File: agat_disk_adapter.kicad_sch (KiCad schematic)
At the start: 10 parts, among them J1 КОНТРОЛЛЕР, J2_A1 ИЗОТ, J2_B2 ИЗОТ, J3 DISK II, J4 GOTEK, J5 Питание GOTEK, J6 ВБ, J7 Джамперы, J8 ВБ2

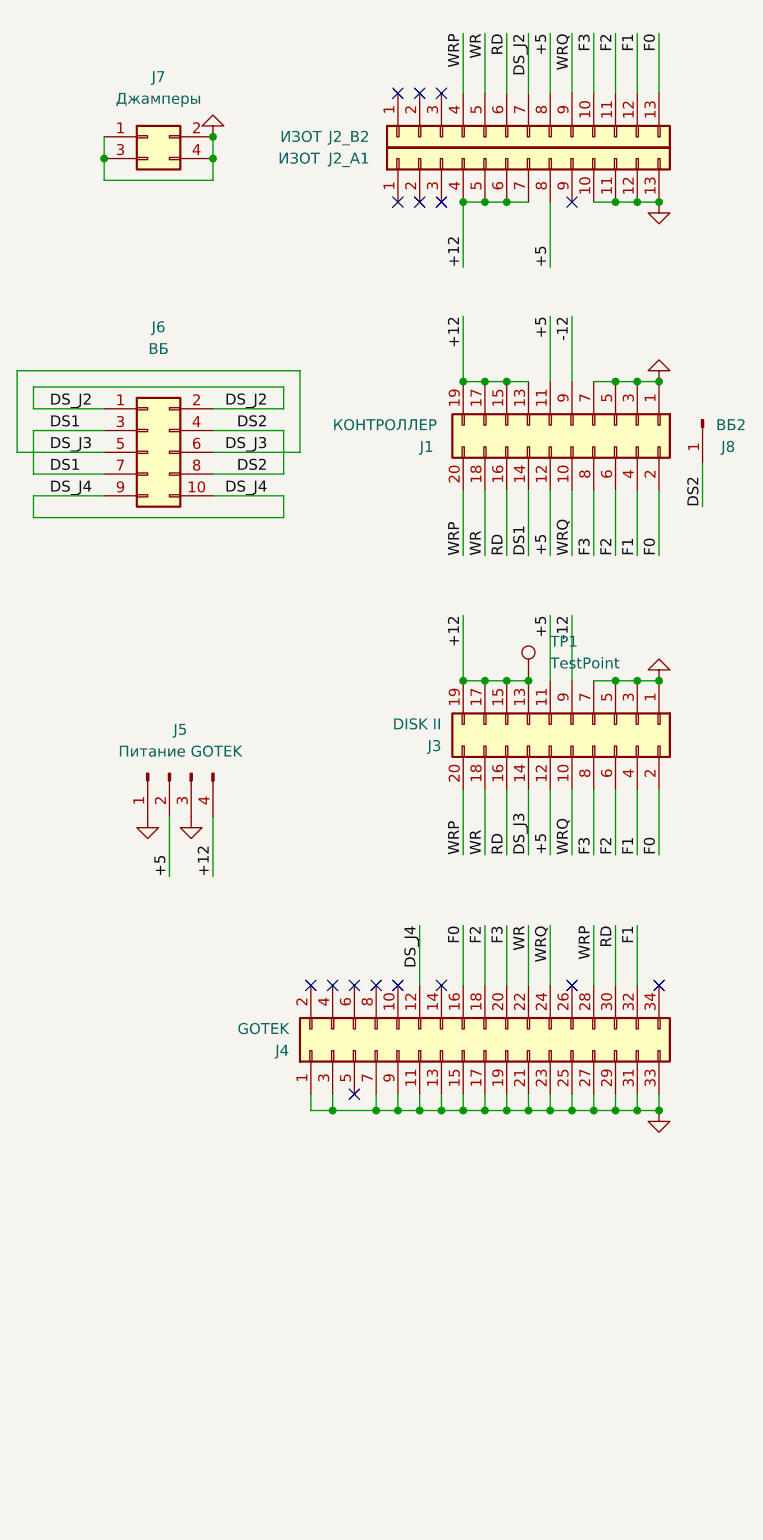
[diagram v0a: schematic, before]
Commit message: one fdc connector
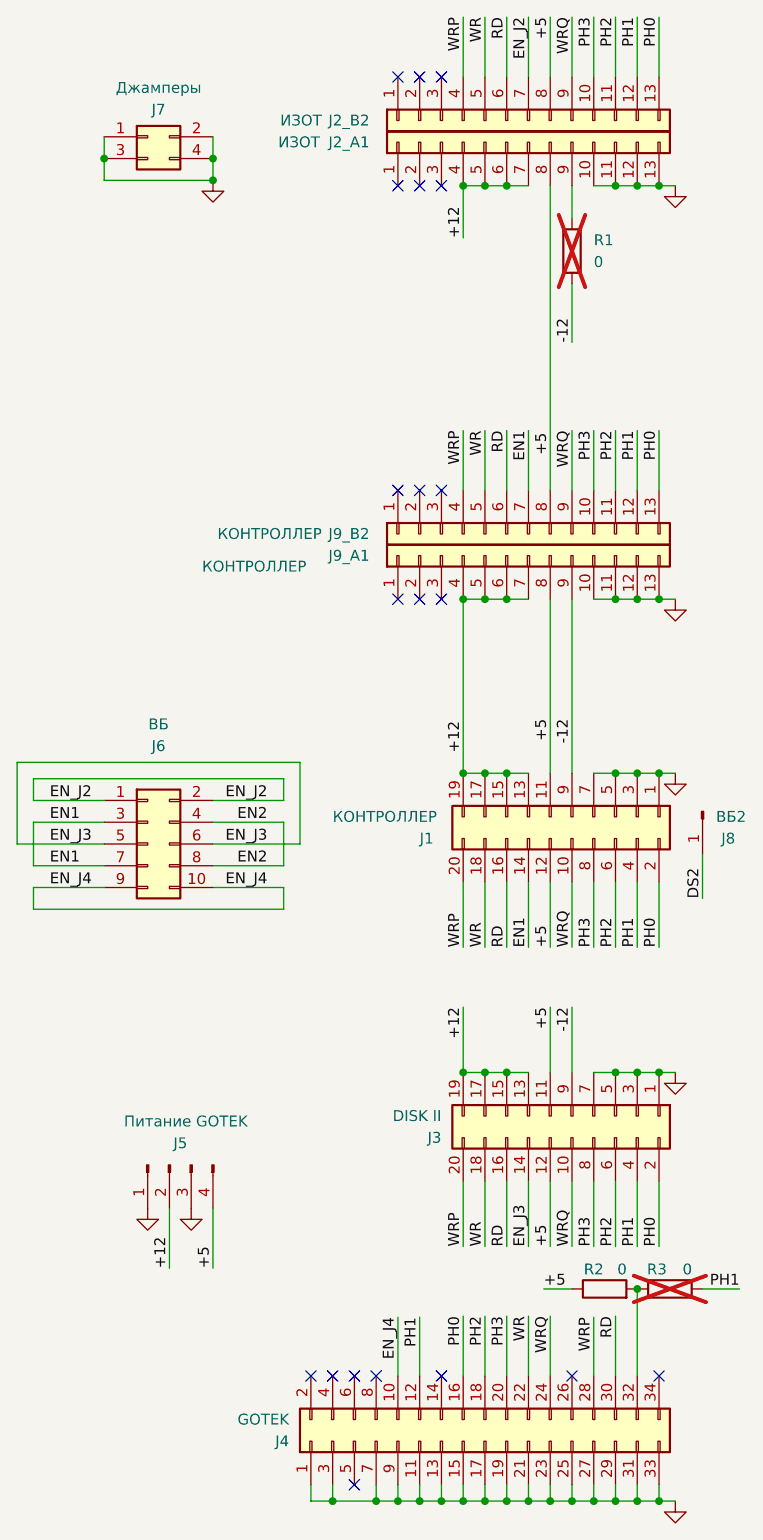
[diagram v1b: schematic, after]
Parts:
- removed TP1: TestPoint, TestPoint:TestPoint_Pad_D3.0mm, symbol Connector:TestPoint
- added J9_A1, J9_B2: КОНТРОЛЛЕР, Connector_JST:JST_EH_B13B-EH-A_1x13_P2.50mm_Vertical, symbol Connector_Generic:Conn_01x13
- added R1, R2, R3: 0, Resistor_SMD:R_1206_3216Metric, symbol Device:R
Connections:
- net +12: now also J5.2 (Pin_2), J9_A1.4 (Pin_4), J9_A1.5 (Pin_5), J9_A1.6 (Pin_6), J9_A1.7 (Pin_7); no longer J5.4 (Pin_4)
- net +5: now also J5.4 (Pin_4), J9_A1.8 (Pin_8), J9_B2.8 (Pin_8), R2.1; no longer J5.2 (Pin_2)
- net -12: now also J9_A1.9 (Pin_9), R1.2
- net DS2: no longer J6.4 (Pin_4), J6.8 (Pin_8)
- net GND: now also J9_A1.10 (Pin_10), J9_A1.11 (Pin_11), J9_A1.12 (Pin_12), J9_A1.13 (Pin_13)
- net RD: now also J9_B2.6 (Pin_6)
- net WR: now also J9_B2.5 (Pin_5)
- net WRP: now also J9_B2.4 (Pin_4)
- net WRQ: now also J9_B2.9 (Pin_9)
- net EN_J4: now reaches J4.10 (Pin_10)
- net EN_J4: now also J6.10 (Pin_10), J6.9 (Pin_9)
- net at J2_A1.9 (Pin_9): now also R1.1
- net DS1 renamed EN1
- net EN1: now also J9_B2.7 (Pin_7)
- net DS_J2 renamed EN_J2
- net DS_J3 renamed EN_J3
- removed net DS_J4: J4.12 (Pin_12), J6.10 (Pin_10), J6.9 (Pin_9)
- net F0 renamed PH0
- net PH0: now also J9_B2.13 (Pin_13)
- net F1 renamed PH1
- net PH1: now also J4.12 (Pin_12), J9_B2.12 (Pin_12), R3.1; no longer J4.32 (Pin_32)
- net F2 renamed PH2
- net PH2: now also J9_B2.11 (Pin_11)
- net F3 renamed PH3
- net PH3: now also J9_B2.10 (Pin_10)
- new net: J4.32 (Pin_32), R2.2, R3.2
- new net EN2: J6.4 (Pin_4), J6.8 (Pin_8)
- no-connect marks 16 -> 20
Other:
- moved on the sheet: J1, J2_A1, J2_B2, J3, J4, J5, J6, J8
